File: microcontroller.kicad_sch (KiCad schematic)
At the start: 40 parts, among them J1 Conn_02x05_Odd_Even, J7 USB_C_Receptacle_USB2.0_16P, SW1 SW_MEC_5E, U1 STM32H563RITx, U7 AP2112K-3.3, U8 USBLC6-2SC6, Y1 25 MHz

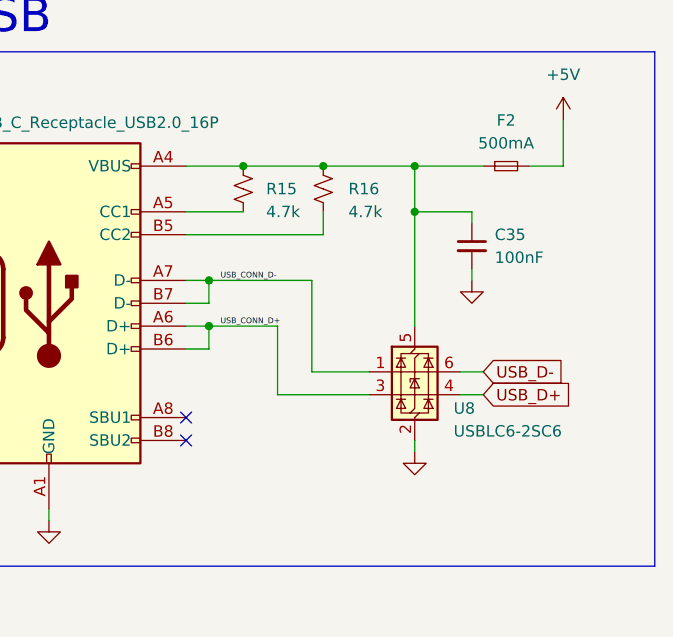
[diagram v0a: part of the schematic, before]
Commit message: Device is a sink not a source
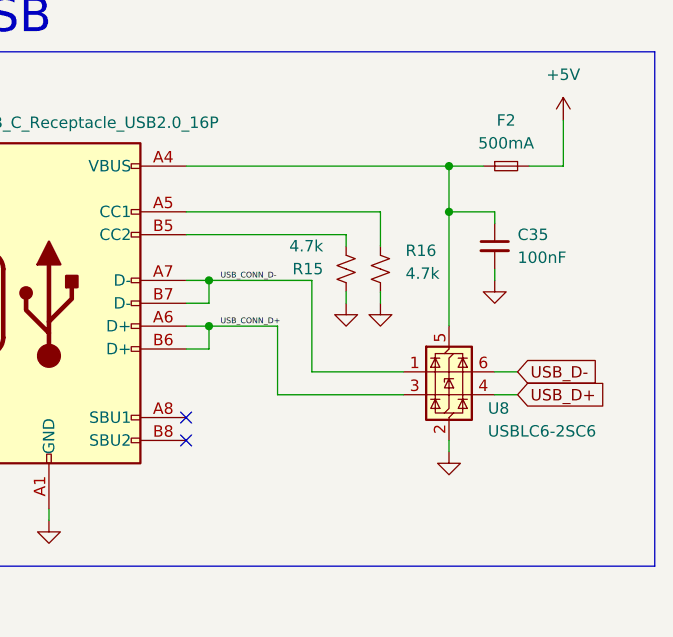
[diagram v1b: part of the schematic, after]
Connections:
- net GND: now also R15.1, R16.2
- net at C35.1, F2.1, J7.A4 (VBUS)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: no longer R15.1, R16.1
- net at R15.2: now also J7.B5 (CC2); no longer J7.A5 (CC1)
- new net: J7.A5 (CC1), R16.1
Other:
- moved on the sheet: C35, R15, R16, U8

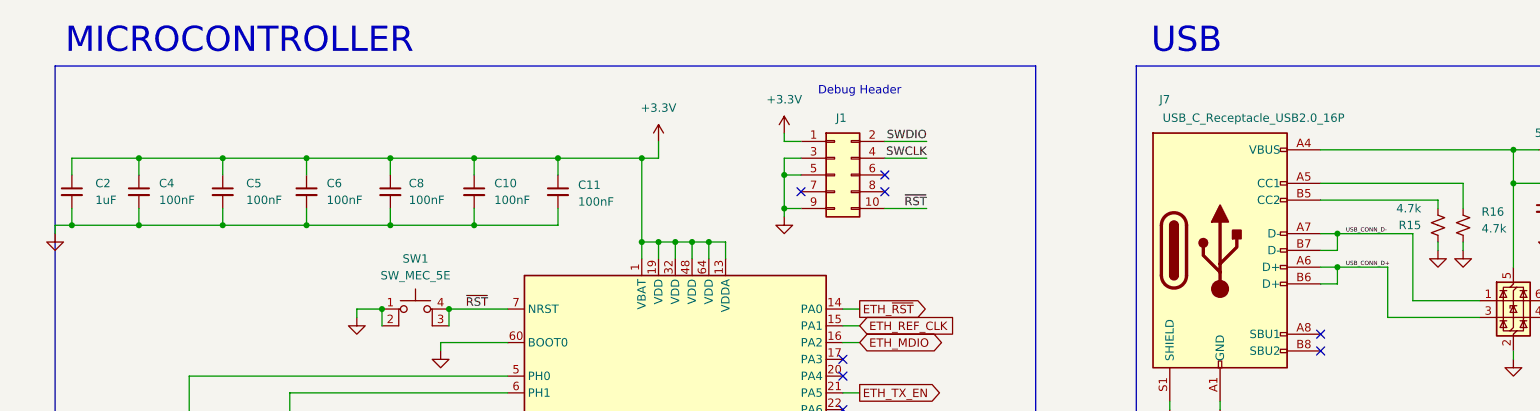
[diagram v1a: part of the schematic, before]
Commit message: Change fuse footprints
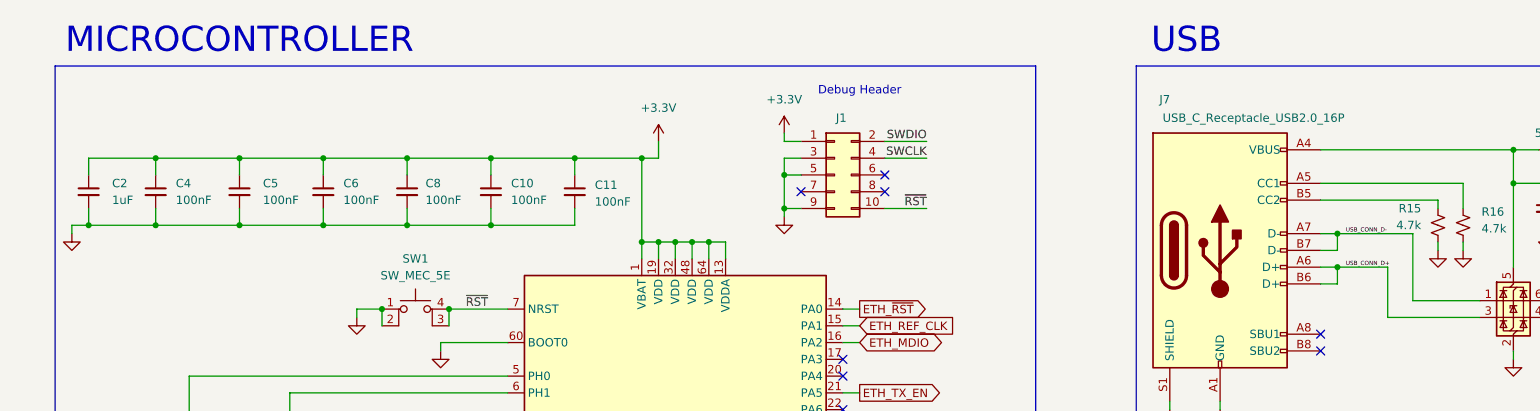
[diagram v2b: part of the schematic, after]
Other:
- moved on the sheet: C10, C11, C2, C4, C5, C6, C8

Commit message: Initial release A1
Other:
- note removed: "Re-check crystal footprint when crystal is chosen"
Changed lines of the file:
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@@
 	(title_block
 		(title "PT DAQ")
-		(date "2026-01-01")
+		(date "2026-01-12")
 		(rev "1A")
 		(company "Aggie Propulsion and Rocketry Lab")

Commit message: Pranked by propfeed and engine again
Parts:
- removed U7: AP2112K-3.3, Package_TO_SOT_SMD:SOT-23-5, symbol Regulator_Linear:AP2112K-3.3
- added U3: TPS7A2045PDBV, Package_TO_SOT_SMD:SOT-23-5, symbol Regulator_Linear:TPS7A20xxxDBV
- renumbered C2 to C1, C3 to C10, C7 to C11, C9 to C12, C29 to C13, C30 to C14, C31 to C15, C32 to C16, C33 to C17, C34 to C18, C4 to C2, C5 to C3, C6 to C4, C8 to C5, C10 to C6, C11 to C7, C35 to C8, C1 to C9, F2 to F1, J7 to J2, R15 to R1, R16 to R2, R1 to R3, R2 to R4, R3 to R5, R12 to R6, R13 to R7, R14 to R8, U8 to U1, U1 to U2
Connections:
- net +3.3V: now also U3.5 (OUT)
- net +5V: now also U3.1 (IN), U3.3 (EN)
- net GND: now also U3.2 (GND)
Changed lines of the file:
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@@
 (kicad_sch
-	(version 20250114)
+	(version 20260306)
 	(generator "eeschema")
-	(generator_version "9.0")
+	(generator_version "10.0")
 	(paper "USLetter")
 	(title_block

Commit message: Fix the regulator label
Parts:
- U3: value TPS7A2045PDBV -> TPS7A2033PDBV

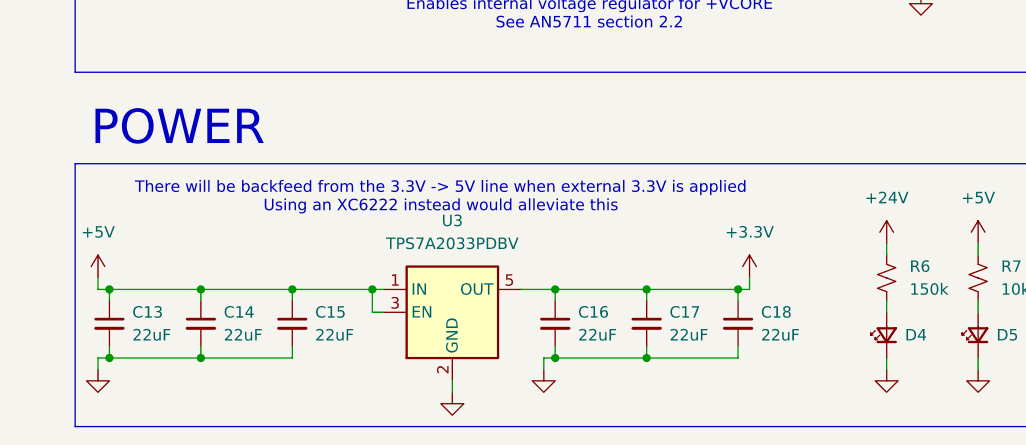
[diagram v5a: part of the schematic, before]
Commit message: Swap TPS7A20 for LP5907 (Daniel yelled at me again)
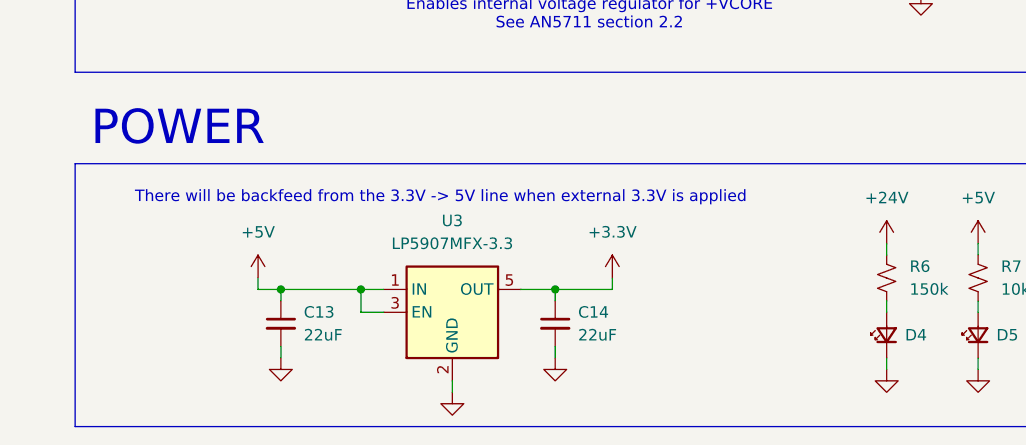
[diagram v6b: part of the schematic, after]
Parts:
- removed C14, C15, C17, C18: 22uF, aprlprints:C_0805-noct, symbol Device:C_Small
- removed U3: TPS7A2033PDBV, Package_TO_SOT_SMD:SOT-23-5, symbol Regulator_Linear:TPS7A20xxxDBV
- added U3: LP5907MFX-3.3, Package_TO_SOT_SMD:SOT-23-5, symbol Regulator_Linear:LP5907MFX-3.3
- renumbered C16 to C14
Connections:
- net +3.3V: now also U3.5 (OUT)
- net +5V: now also U3.1 (IN), U3.3 (EN)
- net GND: now also U3.2 (GND)
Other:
- note added: "There will be backfeed from the 3.3V -> 5V line when external 3.3V is applied"
- note removed: "There will be backfeed from the 3.3V -> 5V line when external 3.3V is applied Using an XC6222 instead would alleviate this"

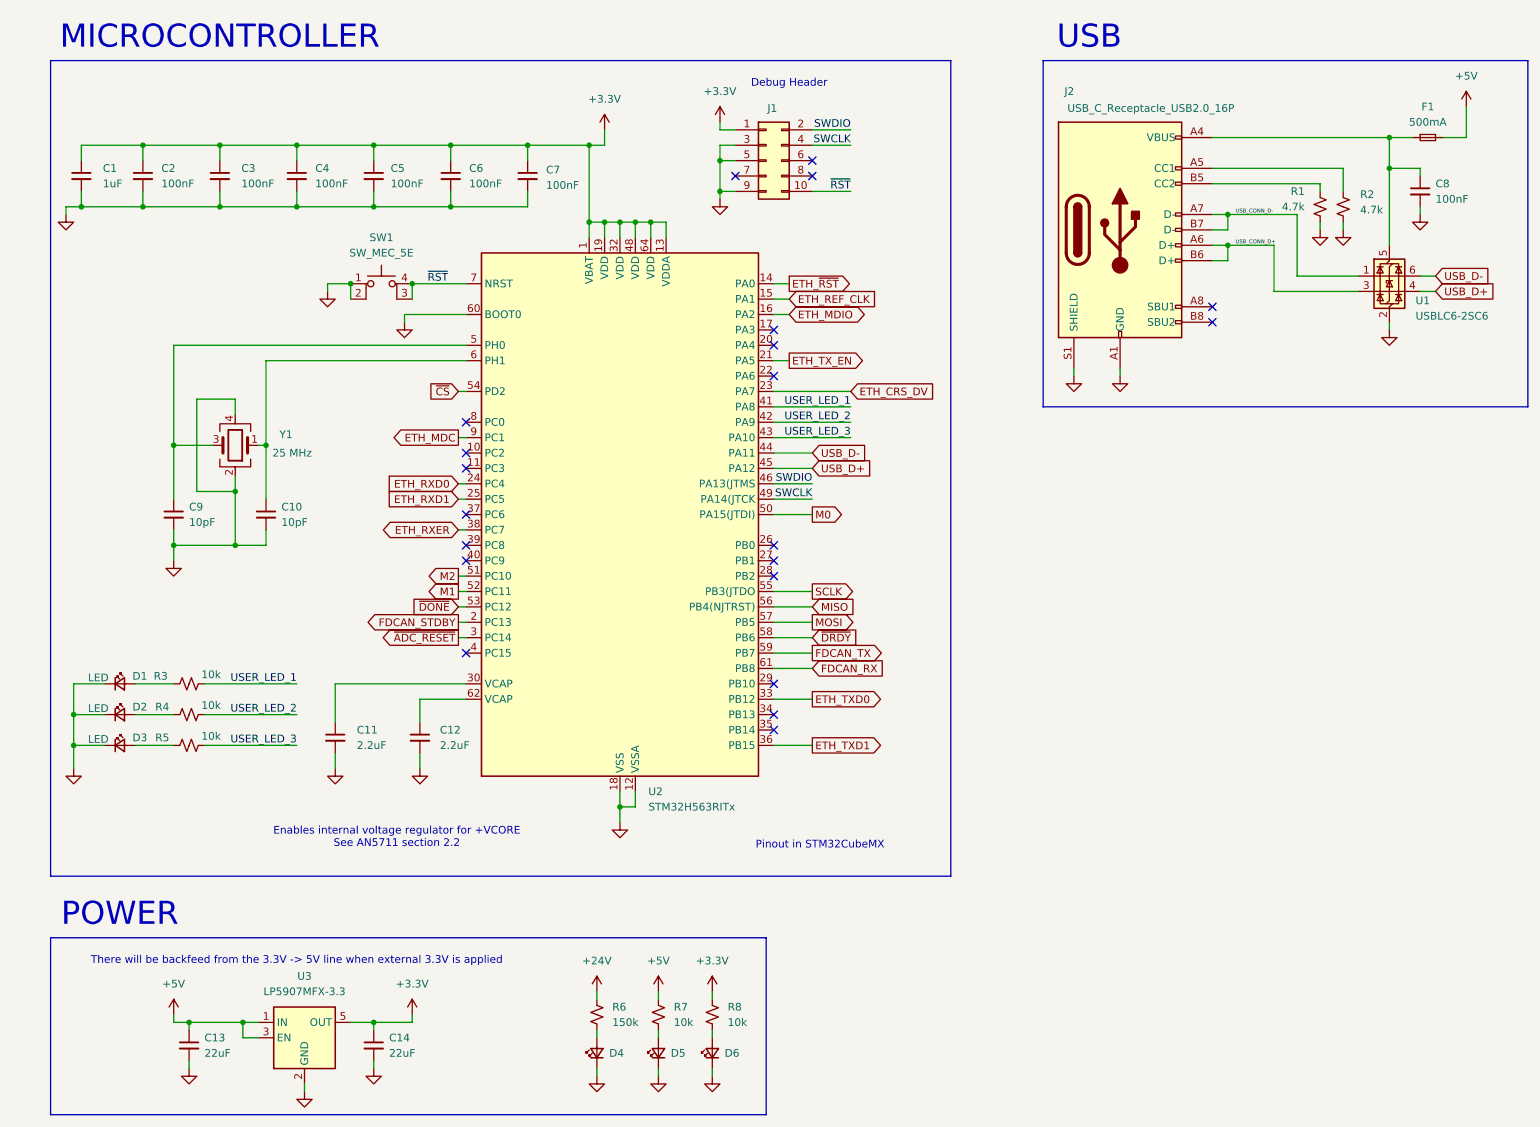
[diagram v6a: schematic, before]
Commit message: Swap to STM32H563RIV6, and add split +3.3V and +3.3VA
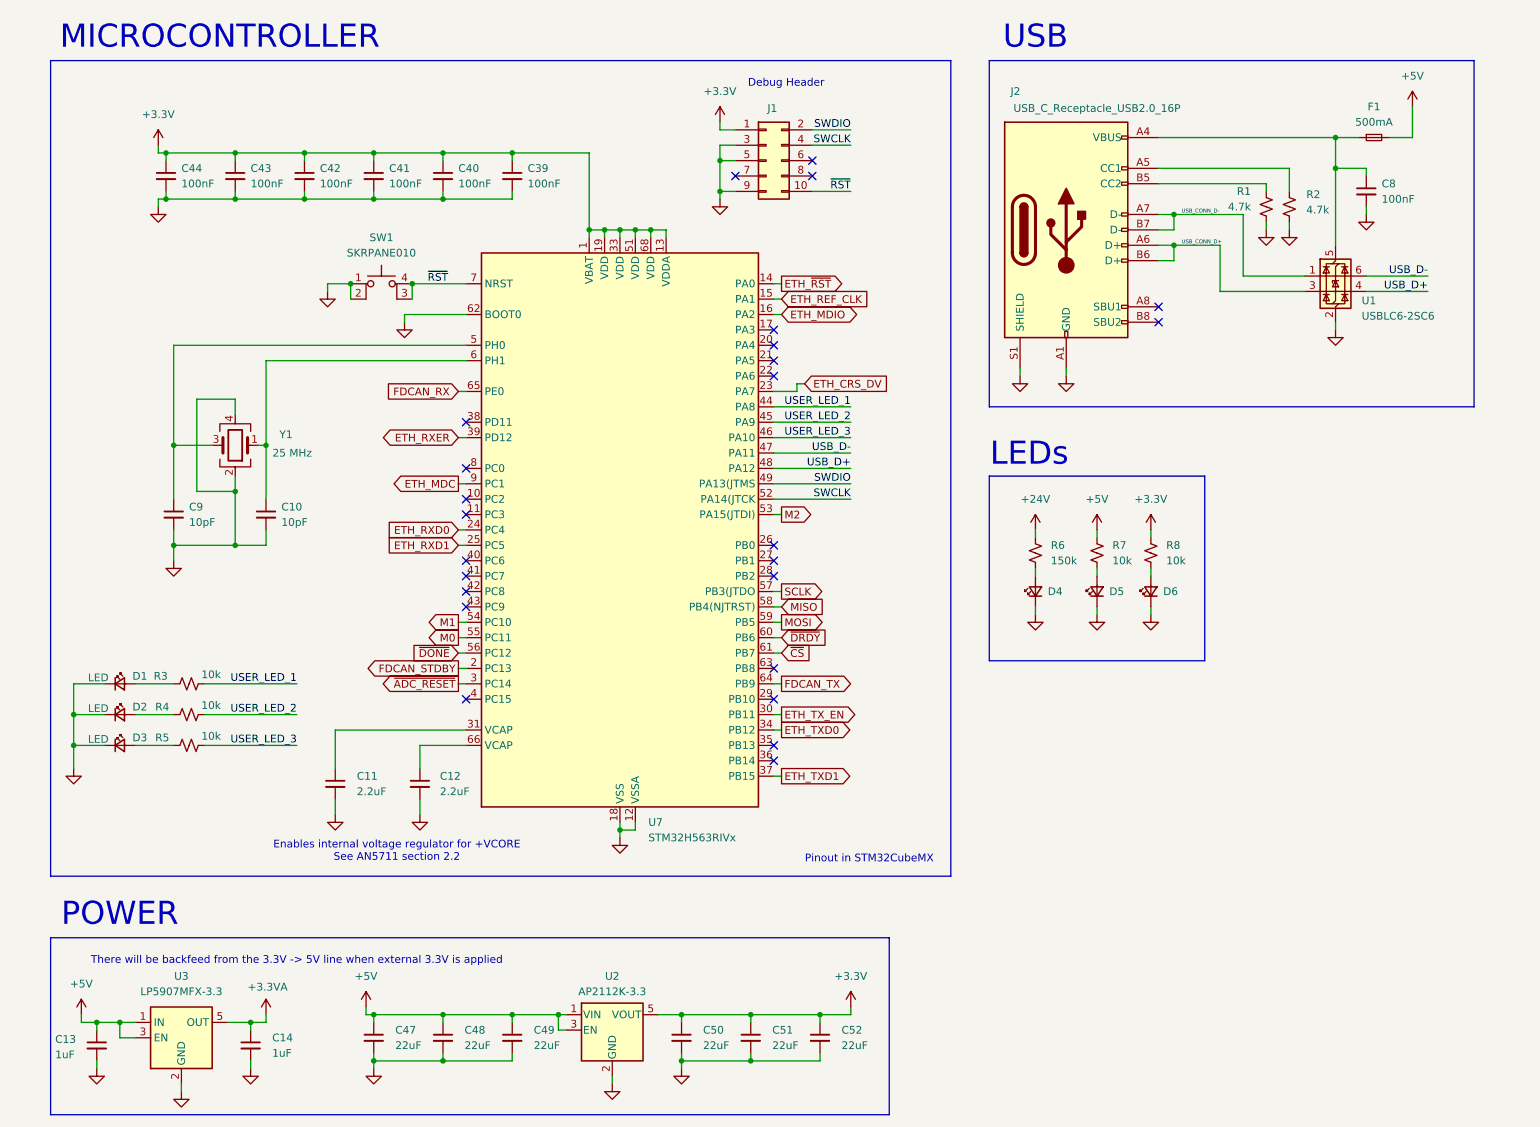
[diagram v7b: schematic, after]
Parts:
- removed C1: 1uF, aprlprints:C_0603-noct, symbol Device:C_Small
- removed C2, C3, C4, C5, C6, C7: 100nF, aprlprints:C_0603-noct, symbol Device:C_Small
- removed U2: STM32H563RITx, Package_QFP:LQFP-64_10x10mm_P0.5mm, symbol MCU_ST_STM32H5:STM32H563RITx
- added C39, C40, C41, C42, C43, C44: 100nF, aprlprints:C_0603-noct, symbol Device:C_Small
- added C47, C48, C49, C50, C51, C52: 22uF, aprlprints:C_0805-noct, symbol Device:C_Small
- added U2: AP2112K-3.3, Package_TO_SOT_SMD:SOT-23-5, symbol Regulator_Linear:AP2112K-3.3
- added U7: STM32H563RIVx, Package_DFN_QFN:QFN-68-1EP_8x8mm_P0.4mm_EP6.4x6.4mm, symbol MCU_ST_STM32H5:STM32H563RIVx
- C13, C14: value 22uF -> 1uF; footprint aprlprints:C_0805-noct -> aprlprints:C_0603-noct; LCSC (none) -> C602037
- SW1: value SW_MEC_5E -> SKRPANE010
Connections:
- net +3.3V: now also C39.1, C40.1, C41.1, C42.1, C43.1, C44.1, C50.1, C51.1, C52.1, U2.5 (VOUT), U7.1 (VBAT), U7.13 (VDDA), U7.19 (VDD), U7.33 (VDD), U7.51 (VDD), U7.68 (VDD); no longer C14.1, U3.5 (OUT)
- net +5V: now also C47.1, C48.1, C49.1, U2.1 (VIN), U2.3 (EN)
- net ETH_CRS_DV: now also U7.23 (PA7)
- net ETH_MDC: now also U7.9 (PC1)
- net ETH_MDIO: now also U7.16 (PA2)
- net ETH_REF_CLK: now also U7.15 (PA1)
- net ETH_RXD0: now also U7.24 (PC4)
- net ETH_RXD1: now also U7.25 (PC5)
- net ETH_RXER: now also U7.39 (PD12)
- net ETH_TXD0: now also U7.34 (PB12)
- net ETH_TXD1: now also U7.37 (PB15)
- net ETH_TX_EN: now also U7.30 (PB11)
- net ETH_~{RST}: now also U7.14 (PA0)
- net FDCAN_RX: now also U7.65 (PE0)
- net FDCAN_STDBY: now also U7.2 (PC13)
- net FDCAN_TX: now also U7.64 (PB9)
- net GND: now also C39.2, C40.2, C41.2, C42.2, C43.2, C44.2, C47.2, C48.2, C49.2, C50.2, C51.2, C52.2, U2.2 (GND), U7.12 (VSSA), U7.18 (VSS), U7.32 (VSS), U7.50 (VSS), U7.62 (BOOT0), U7.67 (VSS), U7.69 (VSS)
- net M0: now also U7.55 (PC11)
- net M1: now also U7.54 (PC10)
- net M2: now also U7.53 (PA15(JTDI))
- net MISO: now also U7.58 (PB4(NJTRST))
- net MOSI: now also U7.59 (PB5)
- net SCLK: now also U7.57 (PB3(JTDO)
- net SWCLK: now also U7.52 (PA14(JTCK)
- net SWDIO: now also U7.49 (PA13(JTMS)
- net USB_D+: now also U7.48 (PA12)
- net USB_D-: now also U7.47 (PA11)
- net USER_LED_1: now also U7.44 (PA8)
- net USER_LED_2: now also U7.45 (PA9)
- net USER_LED_3: now also U7.46 (PA10)
- net ~{ADC_RESET}: now also U7.3 (PC14)
- net ~{CS}: now also U7.61 (PB7)
- net ~{DONE}: now also U7.56 (PC12)
- net ~{DRDY}: now also U7.60 (PB6)
- net ~{RST}: now also U7.7 (NRST)
- net at C11.1: now also U7.31 (VCAP)
- net at C9.1, Y1.3: now also U7.5 (PH0)
- net at C10.1, Y1.1: now also U7.6 (PH1)
- net at C12.1: now also U7.66 (VCAP)
- new net +3.3VA: C14.1, U3.5 (OUT)
- no-connect marks 21 -> 25
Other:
- note added: "LEDs"
- moved on the sheet: C8, D4, D5, D6, F1, J2, R1, R2, R6, R7, R8, U1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

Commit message: June 20th is not real and cant hurt me
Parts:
- C1: renamed from C44; footprint aprlprints:C_0603-noct -> APRLPrints:C_0603
- C10: renamed from C11; footprint aprlprints:C_0603-noct -> APRLPrints:C_0603
- C11: renamed from C12; footprint aprlprints:C_0603-noct -> APRLPrints:C_0603
- C12: renamed from C47; footprint aprlprints:C_0805-noct -> APRLPrints:C_0805
- C13: renamed from C48; footprint aprlprints:C_0805-noct -> APRLPrints:C_0805
- C14: renamed from C49; footprint aprlprints:C_0805-noct -> APRLPrints:C_0805
- C15: renamed from C50; footprint aprlprints:C_0805-noct -> APRLPrints:C_0805
- C16: renamed from C51; footprint aprlprints:C_0805-noct -> APRLPrints:C_0805
- C17: renamed from C52; footprint aprlprints:C_0805-noct -> APRLPrints:C_0805
- C18: renamed from C13; footprint aprlprints:C_0603-noct -> APRLPrints:C_0603
- C19: renamed from C14; footprint aprlprints:C_0603-noct -> APRLPrints:C_0603
- C2: renamed from C43; footprint aprlprints:C_0603-noct -> APRLPrints:C_0603
- C3: renamed from C42; footprint aprlprints:C_0603-noct -> APRLPrints:C_0603
- C4: renamed from C41; footprint aprlprints:C_0603-noct -> APRLPrints:C_0603
- C5: renamed from C40; footprint aprlprints:C_0603-noct -> APRLPrints:C_0603
- C6: renamed from C39; footprint aprlprints:C_0603-noct -> APRLPrints:C_0603
- C7: renamed from C8; footprint aprlprints:C_0603-noct -> APRLPrints:C_0603
- C8: renamed from C9; footprint aprlprints:C_0603-noct -> APRLPrints:C_0603
- C9: renamed from C10; footprint aprlprints:C_0603-noct -> APRLPrints:C_0603
- D1: renamed from D4; footprint aprlprints:LED_0603-noct -> APRLPrints:LED_0603
- D2: renamed from D5; footprint aprlprints:LED_0603-noct -> APRLPrints:LED_0603
- D3: renamed from D6; footprint aprlprints:LED_0603-noct -> APRLPrints:LED_0603
- D4: renamed from D1; footprint aprlprints:LED_0603-noct -> APRLPrints:LED_0603
- D5: renamed from D2; footprint aprlprints:LED_0603-noct -> APRLPrints:LED_0603
- D6: renamed from D3; footprint aprlprints:LED_0603-noct -> APRLPrints:LED_0603
- F1: footprint Fuse:Fuse_0805_2012Metric -> APRLPrints:Fuse_0805_2012Metric
- R1, R2: footprint aprlprints:R_0603-noct -> APRLPrints:R_0603
- R3: renamed from R6; footprint aprlprints:R_0603-noct -> APRLPrints:R_0603
- R4: renamed from R7; footprint aprlprints:R_0603-noct -> APRLPrints:R_0603
- R5: renamed from R8; footprint aprlprints:R_0603-noct -> APRLPrints:R_0603
- R6: renamed from R3; footprint aprlprints:R_0603-noct -> APRLPrints:R_0603
- R7: renamed from R4; footprint aprlprints:R_0603-noct -> APRLPrints:R_0603
- R8: renamed from R5; footprint aprlprints:R_0603-noct -> APRLPrints:R_0603
- SW1: footprint aprlprints:SKRPANE010-noct -> APRLPrints:SKRPANE010
- Y1: footprint aprlprints:3225-4P-L-noct -> APRLPrints:3225-4P-L
- renumbered U7 to U2, U2 to U3, U3 to U4
